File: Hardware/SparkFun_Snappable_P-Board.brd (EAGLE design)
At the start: 129.5 x 66 mm, 128 parts

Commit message: Ready for protos
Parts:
- moved LOGO1 127.3 mm to (0.38, 0.13)
- moved LOGO2 127.3 mm to (1.91, 0.13)
- moved JP84 3.59 mm to (80.0, 44.5)
- moved JP91 3.59 mm to (80.0, 26.7)
- moved JP95 3.59 mm to (80.0, 16.5)
- moved JP96 3.59 mm to (80.0, 14.0)
- moved JP98 3.59 mm to (80.0, 8.89)
- moved JP100 3.59 mm to (80.0, 3.81)
- moved JP9 3.59 mm to (3.81, 44.5)
- moved JP34 3.59 mm to (29.2, 44.5)
- moved JP59 3.59 mm to (54.6, 44.5)
- moved JP76 3.59 mm to (80.0, 64.8)
- moved JP77 3.59 mm to (80.0, 62.2)
- moved JP78 3.59 mm to (80.0, 59.7)
- moved JP79 3.59 mm to (80.0, 57.1)
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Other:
- board size 129.5 x 66 mm -> 129.5 x 68.6 mm
- board text added: "-"
- board text added: "B"
- board text added: "F"
- board text added: "P"
- board text added: "S"
- board text added: "a"
- board text added: "b"
- board text added: "d"
- board text added: "e"
- board text added: "k"
- board text added: "l"
- board text added: "n"
- board text added: "o"
- board text added: "p"
- board text added: "r"
- board text added: "u"
- board text removed: "Snappable P-Board"

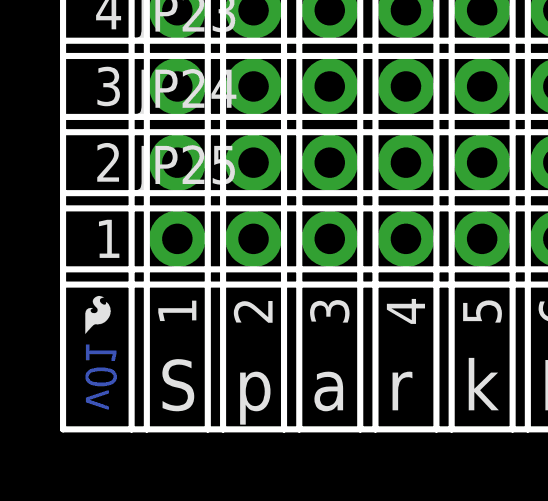
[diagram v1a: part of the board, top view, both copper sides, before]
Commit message: Fixed logo line thickness
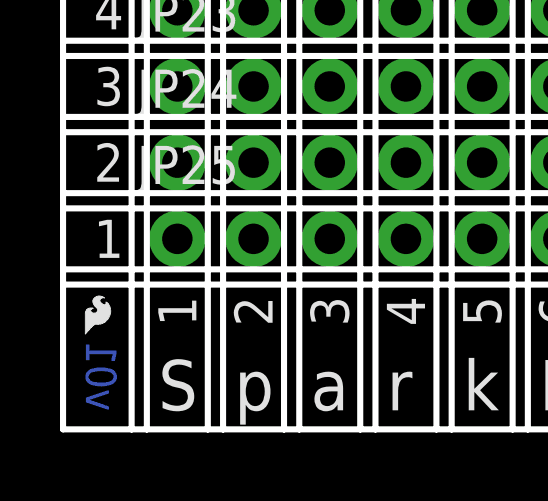
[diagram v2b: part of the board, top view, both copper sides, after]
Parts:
- JP1, JP10, JP100, JP101, JP102, JP103, JP104, JP105, JP106, JP107, JP108, JP109, JP11, JP110, JP111, JP112, JP113, JP114, JP115, JP116, JP117, JP118, JP119, JP12, JP120, JP121, JP122, JP123, JP124, JP125, JP13, JP14, JP15, JP16, JP17, JP18, JP19, JP2, JP20, JP21, JP22, JP23, JP24, JP25, JP26, JP27, JP28, JP29, JP3, JP30, JP31, JP32, JP33, JP34, JP35, JP36, JP37, JP38, JP39, JP4, JP40, JP41, JP42, JP43, JP44, JP45, JP46, JP47, JP48, JP49, JP5, JP50, JP51, JP52, JP53, JP54, JP55, JP56, JP57, JP58, JP59, JP6, JP60, JP61, JP62, JP63, JP64, JP65, JP66, JP67, JP68, JP69, JP7, JP70, JP71, JP72, JP73, JP74, JP75, JP76, JP77, JP78, JP79, JP8, JP80, JP81, JP82, JP83, JP84, JP85, JP86, JP87, JP88, JP89, JP9, JP90, JP91, JP92, JP93, JP94, JP95, JP96, JP97, JP98, JP99: value M10NO_SILK_PTH_FEMALE -> (none)
